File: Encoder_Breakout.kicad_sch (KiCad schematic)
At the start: 4 parts, among them J1 5-104363-1, J2 Conn_02x07_Odd_Even, J5 5-104935-3, J6 5-104363-1

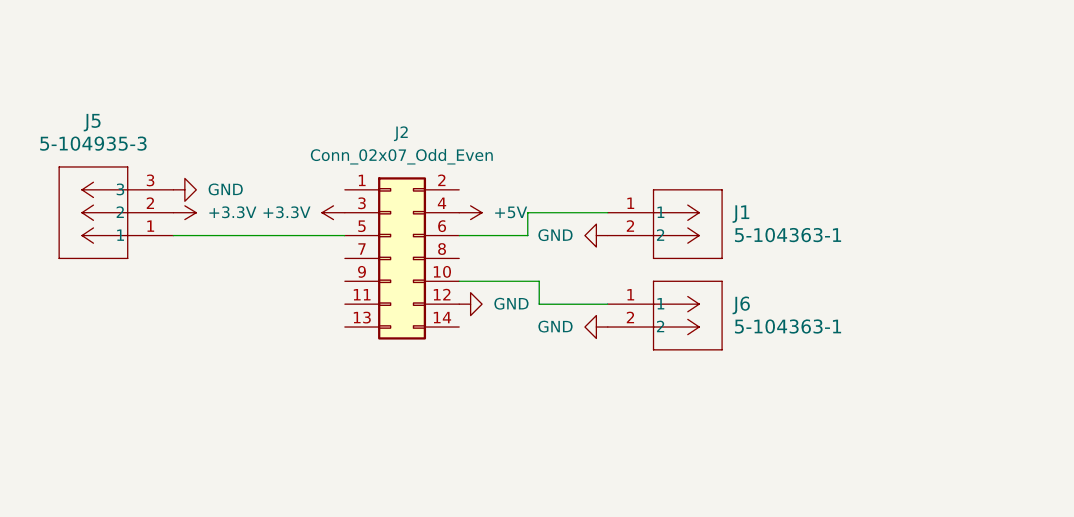
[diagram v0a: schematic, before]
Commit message: Reshape to sparkmax and add LEDs
Signed-off-by: Colin <cfinn68916@gmail.com>
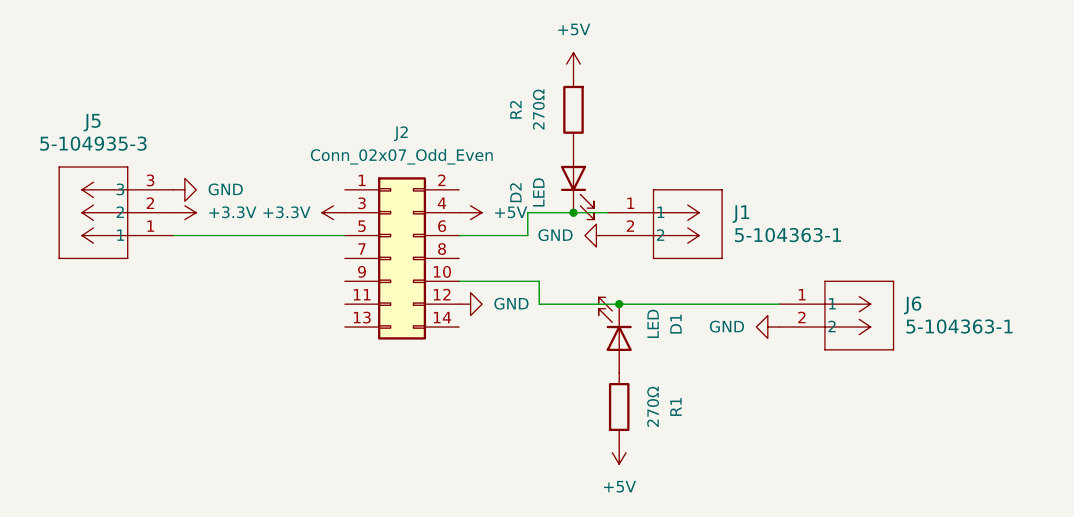
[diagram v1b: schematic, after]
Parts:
- added D1, D2: LED, LED_SMD:LED_0603_1608Metric, symbol Device:LED
- added R1, R2: 270Ω, Resistor_SMD:R_0603_1608Metric, symbol Device:R
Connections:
- net +5V: now also R1.2, R2.2
- net at J1.1, J2.6 (Pin_6): now also D2.1 (K)
- net at J2.10 (Pin_10), J6.1: now also D1.1 (K)
- new net: D2.2 (A), R2.1
- new net: D1.2 (A), R1.1
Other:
- moved on the sheet: J6
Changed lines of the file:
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@@
 (kicad_sch (version 20230121) (generator eeschema)
   (paper "A4")
-  (wire (pts (xy 154.94 87.63) (xy 162.56 87.63))
+  (junction (at 158.75 77.47) (diameter 0) (color 0 0 0 0)
+  )
+  (junction (at 163.83 87.63) (diameter 0) (color 0 0 0 0)
+  )
+  (wire (pts (xy 154.94 87.63) (xy 163.83 87.63))
     (stroke (width 0) (type default))
   )
@@
     (stroke (width 0) (type default))
   )
-  (wire (pts (xy 153.67 77.47) (xy 162.56 77.47))
+  (wire (pts (xy 158.75 77.47) (xy 162.56 77.47))
+    (stroke (width 0) (type default))
+  )
+  (wire (pts (xy 153.67 77.47) (xy 158.75 77.47))
+    (stroke (width 0) (type default))
+  )
+  (wire (pts (xy 163.83 87.63) (xy 181.61 87.63))
     (stroke (width 0) (type default))
   )
@@
     )
   )
+  (symbol (lib_id "Device:LED") (at 158.75 73.66 90) (unit 1)
+    (in_bom yes) (on_board yes) (dnp no) (fields_autoplaced)
+    (property "Reference" "D2" (at 152.4 75.2475 0)
+      (effects (font (size 1.27 1.27)))
+    )
+    (property "Value" "LED" (at 154.94 75.2475 0)
+      (effects (font (size 1.27 1.27)))
+    )
+    (property "Footprint" "LED_SMD:LED_0603_1608Metric" (at 158.75 73.66 0)
+      (effects (font (size 1.27 1.27)) hide)
+    )
+    (property "Datasheet" "~" (at 158.75 73.66 0)
+      (effects (font (size 1.27 1.27)) hide)
+    )
+    (pin "1")
+    (pin "2")
+    (instances
+      (project "Encoder_Breakout"
+        (path "/896045ed-d89c-42ad-9d47-a66b46c2187b"
+          (reference "D2") (unit 1)
+        )
+      )
+    )
+  )
   (symbol (lib_id "2023-10-03_23-14-34:5-104363-1") (at 162.56 77.47 0) (unit 1)
     (in_bom yes) (on_board yes) (dnp no) (fields_autoplaced)
@@
         (path "/896045ed-d89c-42ad-9d47-a66b46c2187b"
           (reference "#PWR01") (unit 1)
+        )
+      )
+    )
+  )
+  (symbol (lib_id "power:+5V") (at 158.75 62.23 0) (unit 1)
+    (in_bom yes) (on_board yes) (dnp no) (fields_autoplaced)
+    (property "Reference" "#PWR09" (at 158.75 66.04 0)
+      (effects (font (size 1.27 1.27)) hide)
+    )
+    (property "Value" "+5V" (at 158.75 57.15 0)
+      (effects (font (size 1.27 1.27)))
+    )
+    (property "Footprint" "" (at 158.75 62.23 0)
+      (effects (font (size 1.27 1.27)) hide)
+    )
+    (property "Datasheet" "" (at 158.75 62.23 0)
+      (effects (font (size 1.27 1.27)) hide)
+    )
+    (pin "1")
+    (instances
+      (project "Encoder_Breakout"
+        (path "/896045ed-d89c-42ad-9d47-a66b46c2187b"
+          (reference "#PWR09") (unit 1)
         )
       )
@@
     )
   )
-  (symbol (lib_id "power:GND") (at 162.56 90.17 270) (unit 1)
-    (in_bom yes) (on_board yes) (dnp no) (fields_autoplaced)
-    (property "Reference" "#PWR06" (at 156.21 90.17 0)
-      (effects (font (size 1.27 1.27)) hide)
-    )
-    (property "Value" "GND" (at 158.75 90.17 90)
+  (symbol (lib_id "power:GND") (at 181.61 90.17 270) (unit 1)
+    (in_bom yes) (on_board yes) (dnp no) (fields_autoplaced)
+    (property "Reference" "#PWR06" (at 175.26 90.17 0)
+      (effects (font (size 1.27 1.27)) hide)
+    )
+    (property "Value" "GND" (at 177.8 90.17 90)
       (effects (font (size 1.27 1.27)) (justify right))
     )
-    (property "Footprint" "" (at 162.56 90.17 0)
-      (effects (font (size 1.27 1.27)) hide)
-    )
-    (property "Datasheet" "" (at 162.56 90.17 0)
+    (property "Footprint" "" (at 181.61 90.17 0)
+      (effects (font (size 1.27 1.27)) hide)
+    )
+    (property "Datasheet" "" (at 181.61 90.17 0)
       (effects (font (size 1.27 1.27)) hide)
     )
@@
     )
   )
+  (symbol (lib_id "power:+5V") (at 163.83 102.87 180) (unit 1)
+    (in_bom yes) (on_board yes) (dnp no) (fields_autoplaced)
+    (property "Reference" "#PWR08" (at 163.83 99.06 0)
+      (effects (font (size 1.27 1.27)) hide)
+    )
+    (property "Value" "+5V" (at 163.83 107.95 0)
+      (effects (font (size 1.27 1.27)))
+    )
+    (property "Footprint" "" (at 163.83 102.87 0)
+      (effects (font (size 1.27 1.27)) hide)
+    )
+    (property "Datasheet" "" (at 163.83 102.87 0)
+      (effects (font (size 1.27 1.27)) hide)
+    )
+    (pin "1")
+    (instances
+      (project "Encoder_Breakout"
+        (path "/896045ed-d89c-42ad-9d47-a66b46c2187b"
+          (reference "#PWR08") (unit 1)
+        )
+      )
+    )
+  )
+  (symbol (lib_id "Device:R") (at 163.83 99.06 0) (unit 1)
+    (in_bom yes) (on_board yes) (dnp no) (fields_autoplaced)
+    (property "Reference" "R1" (at 170.18 99.06 90)
+      (effects (font (size 1.27 1.27)))
+    )
+    (property "Value" "270Ω" (at 167.64 99.06 90)
+      (effects (font (size 1.27 1.27)))
+    )
+    (property "Footprint" "Resistor_SMD:R_0603_1608Metric" (at 162.052 99.06 90)
+      (effects (font (size 1.27 1.27)) hide)
+    )
+    (property "Datasheet" "~" (at 163.83 99.06 0)
+      (effects (font (size 1.27 1.27)) hide)
+    )
+    (pin "1")
+    (pin "2")
+    (instances
+      (project "Encoder_Breakout"
+        (path "/896045ed-d89c-42ad-9d47-a66b46c2187b"
+          (reference "R1") (unit 1)
+        )
+      )
+    )
+  )
   (symbol (lib_id "power:GND") (at 146.05 87.63 90) (unit 1)
     (in_bom yes) (on_board yes) (dnp no) (fields_autoplaced)
@@
     )
   )
-  (symbol (lib_id "2023-10-03_23-14-34:5-104363-1") (at 162.56 87.63 0) (unit 1)
-    (in_bom yes) (on_board yes) (dnp no) (fields_autoplaced)
-    (property "Reference" "J6" (at 176.53 87.63 0)
+  (symbol (lib_id "2023-10-03_23-14-34:5-104363-1") (at 181.61 87.63 0) (unit 1)
+    (in_bom yes) (on_board yes) (dnp no) (fields_autoplaced)
+    (property "Reference" "J6" (at 195.58 87.63 0)
       (effects (font (size 1.524 1.524)) (justify left))
     )
-    (property "Value" "5-104363-1" (at 176.53 90.17 0)
+    (property "Value" "5-104363-1" (at 195.58 90.17 0)
       (effects (font (size 1.524 1.524)) (justify left))
     )
-    (property "Footprint" "CONN_5-104363-1_TYCO" (at 162.56 87.63 0)
-      (effects (font (size 1.27 1.27) italic) hide)
-    )
-    (property "Datasheet" "5-104363-1" (at 162.56 87.63 0)
+    (property "Footprint" "CONN_5-104363-1_TYCO" (at 181.61 87.63 0)
+      (effects (font (size 1.27 1.27) italic) hide)
+    )
+    (property "Datasheet" "5-104363-1" (at 181.61 87.63 0)
       (effects (font (size 1.27 1.27) italic) hide)
     )
@@
         )
       )
+    )
+  )
+  (symbol (lib_id "Device:LED") (at 163.83 91.44 270) (unit 1)
+    (in_bom yes) (on_board yes) (dnp no) (fields_autoplaced)
+    (property "Reference" "D1" (at 170.18 89.8525 0)
+      (effects (font (size 1.27 1.27)))
+    )
+    (property "Value" "LED" (at 167.64 89.8525 0)
+      (effects (font (size 1.27 1.27)))
+    )
+    (property "Footprint" "LED_SMD:LED_0603_1608Metric" (at 163.83 91.44 0)
+      (effects (font (size 1.27 1.27)) hide)
+    )
+    (property "Datasheet" "~" (at 163.83 91.44 0)
+      (effects (font (size 1.27 1.27)) hide)
+    )
+    (pin "1")
+    (pin "2")
+    (instances
+      (project "Encoder_Breakout"
+        (path "/896045ed-d89c-42ad-9d47-a66b46c2187b"
+          (reference "D1") (unit 1)
+        )
+      )
+    )
+  )
+  (symbol (lib_id "Device:R") (at 158.75 66.04 180) (unit 1)
+    (in_bom yes) (on_board yes) (dnp no) (fields_autoplaced)
+    (property "Reference" "R2" (at 152.4 66.04 90)
+      (effects (font (size 1.27 1.27)))
+    )
+    (property "Value" "270Ω" (at 154.94 66.04 90)
+      (effects (font (size 1.27 1.27)))
+    )
+    (property "Footprint" "Resistor_SMD:R_0603_1608Metric" (at 160.528 66.04 90)
+      (effects (font (size 1.27 1.27)) hide)
+    )
+    (property "Datasheet" "~" (at 158.75 66.04 0)
+      (effects (font (size 1.27 1.27)) hide)
+    )
+    (pin "1")
+    (pin "2")
+    (instances
+      (project "Encoder_Breakout"
+        (path "/896045ed-d89c-42ad-9d47-a66b46c2187b"
+          (reference "R2") (unit 1)
+        )
+      )

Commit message: Remove limit switches
Signed-off-by: Colin <cfinn68916@gmail.com>
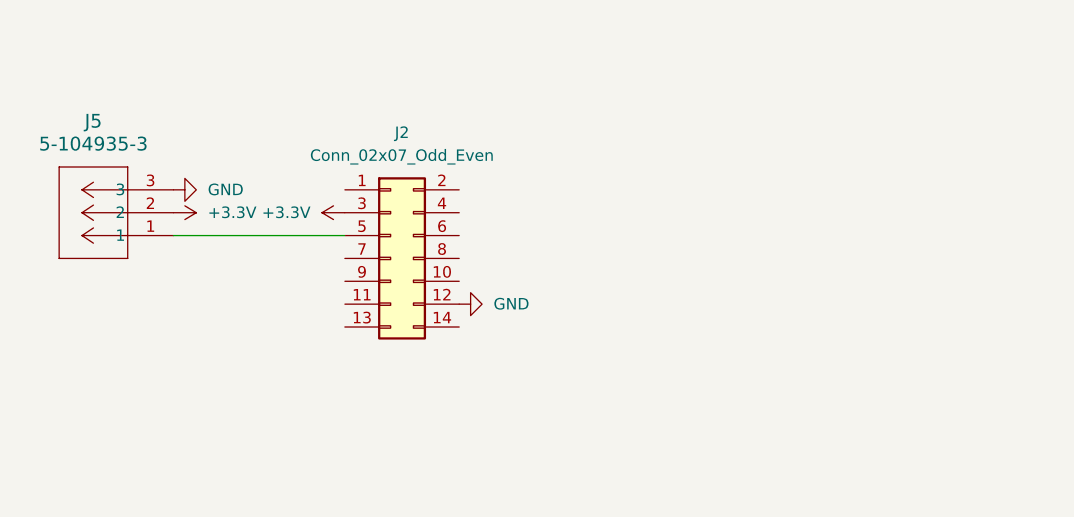
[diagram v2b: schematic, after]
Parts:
- removed D1, D2: LED, LED_SMD:LED_0603_1608Metric, symbol Device:LED
- removed J1, J6: 5-104363-1, CONN_5-104363-1_TYCO, symbol 2023-10-03_23-14-34:5-104363-1
- removed R1, R2: 270Ω, Resistor_SMD:R_0603_1608Metric, symbol Device:R
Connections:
- net +5V: no longer names the net of J2.4 (Pin_4)
